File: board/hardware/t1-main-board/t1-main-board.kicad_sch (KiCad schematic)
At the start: 0 parts

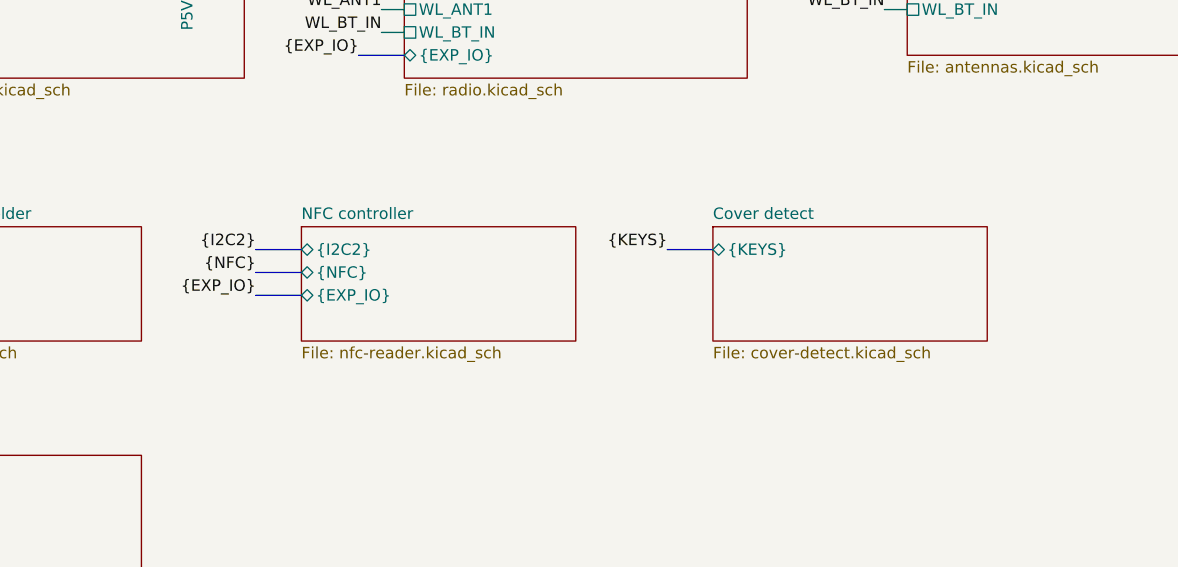
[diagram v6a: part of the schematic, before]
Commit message: NFC reader withdrawn from the board, every model (BRD-057)
Maintainer decision 2026-10-27, reason: board area. blk.nfc-reader (#42)
withdrawn: PN7160, front end, crystal, antenna contacts, NFC_VBAT switch
and link #18 removed (35 parts). BRD-057 reworded: NFC as the dynamic tag
only; blk.nfc-tag stays. Pinout v1: 1N20, A37, B38 become unconnected
spares, expander P05 a spare. BOM v1.18 item 7 (line 50: 5 switches,
lines 127-128 withdrawn), power tree v0.10, variant files, feature blocks.

Sheets after the removed one move up a page; references renumbered in
plan.py, parts.py and the specs (J6201 -> J6101 and others).

Placement v1.4: 990 parts placed, board need 96.9 % (99.1 % before),
factor 1.72; 243 capacitors within bound; DRC 0 errors; ERC 0 errors;
craft Q1 met; overlaps 0; pcb tests pass; STEP exported.

Co-Authored-By: Claude Opus 5.5 <noreply@anthropic.com>
Claude-Session: https://claude.ai/code/session_01Ei262h3TpgY9vyfNLMi5Mn
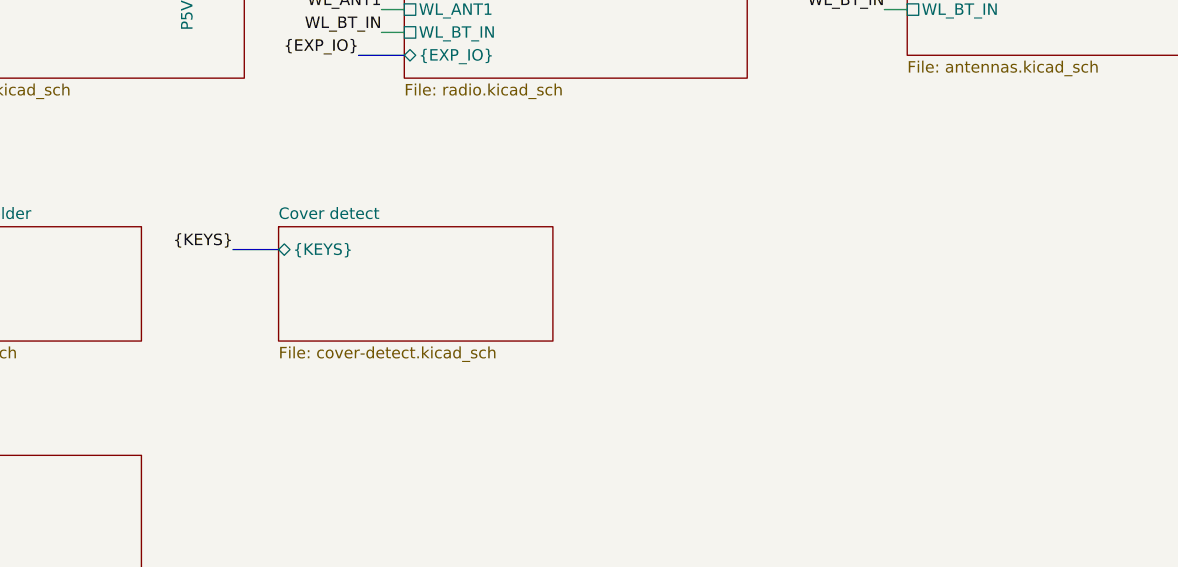
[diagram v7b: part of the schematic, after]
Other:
- removed sheet NFC controller

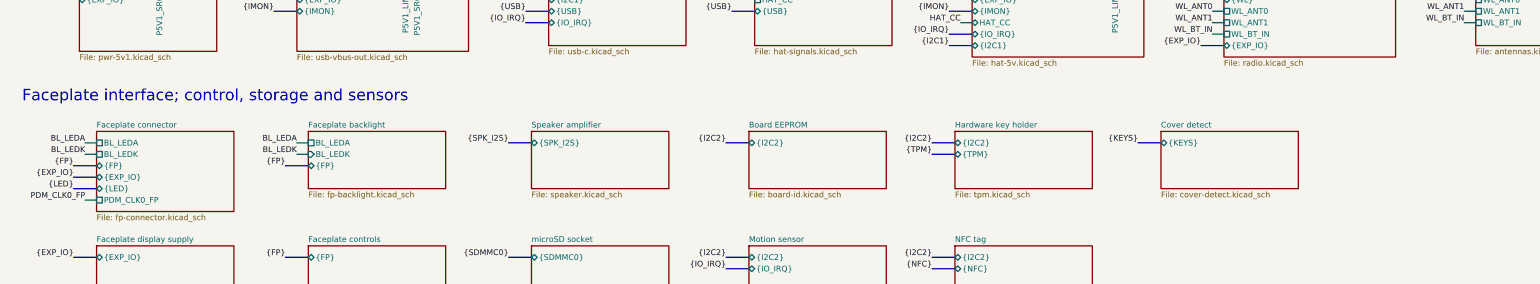
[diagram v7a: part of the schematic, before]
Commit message: Shield-can frames on the back (BOM v1.19, placement v1.6)
blk.shields: three etched two-piece frames made to order under the
amended T1-038, not fitted in either variant: SoC and LPDDR4X, the radio
module, the DACs and the back of the headphone stage. shields.toml holds
the geometry; pcb/shields.py derives land, keep-outs and courtyard ring;
the generator draws the lands and the placer reserves them, with parts up
to 1.3 mm inside (PCB-Z-01). The sheet takes page 59, so the sheets from
fp-display on carry the next page (J6201, SW6901-SW6904).

Placement v1.6: 994 parts placed, 99.5 % board need (97.0 % before the
frames), factor 1.64, 244 capacitors within their bound, DRC 0 errors,
ERC 0 errors, craft Q1 met, pcb tests pass (31), STEP exported.

Co-Authored-By: Claude Opus 5.5 <noreply@anthropic.com>
Claude-Session: https://claude.ai/code/session_013P6pW9LdyEMFishwCcZGUr
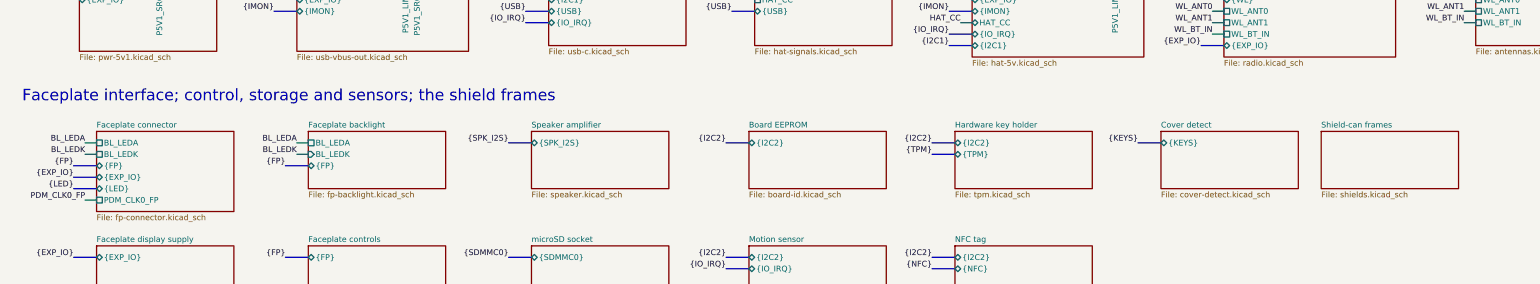
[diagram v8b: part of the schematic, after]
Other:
- added sheet Shield-can frames (shields.kicad_sch)
- note added: "Faceplate interface; control, storage and sensors; the shield frames"
- note removed: "Faceplate interface; control, storage and sensors"
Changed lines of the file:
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@@
 (text "SoC, memory, the coprocessor and MaskROM entry; audio, from the DACs to the jacks; instrumentation and debug" (exclude_from_sim no) (at 25.4 81.28 0) (effects (font (size 2.54 2.54)) (justify left bottom)))
 (text "USB ports (the 5.1 V source, USB-C, the HAT port) and the radio" (exclude_from_sim no) (at 25.4 162.56 0) (effects (font (size 2.54 2.54)) (justify left bottom)))
-(text "Faceplate interface; control, storage and sensors" (exclude_from_sim no) (at 25.4 207.01 0) (effects (font (size 2.54 2.54)) (justify left bottom)))
+(text "Faceplate interface; control, storage and sensors; the shield frames" (exclude_from_sim no) (at 25.4 207.01 0) (effects (font (size 2.54 2.54)) (justify left bottom)))
 (text_box "Notes\n1. Reading order: overviews first, then blocks left to right as power and signals flow;\n   page numbers follow it (CRAFT-111). The SoC's sub-sheets follow the SoC.\n2. Rails cross the hierarchy as power symbols named as the power tree; signals as sheet pins\n   named as each block's interface (CRAFT-112). Buses cross as one bus pin through the\n   project's bus aliases (DDR_CHA, DDR_CHB, EMMC); their members keep their names.\n3. Every block in use has a sheet; a net with a single pin by design ends in a local label." (exclude_from_sim no) (at 300.99 86.36 0) (size 99.06 19.05) (margins 1.905 1.905 1.905 1.905) (stroke (width 0) (type default)) (fill (type none)) (effects (font (size 1.27 1.27)) (justify left top)))
 (sheet (at 25.4 50.8) (size 30.48 12.7) (exclude_from_sim no) (in_bom yes) (on_board yes) (dnp no) (fields_autoplaced yes) (stroke (width 0.1524) (type solid)) (fill (color 0 0 0 0.0000))
@@
   (property "Block" "blk.fp-display" (at 41.91 254.588 0) (effects (font (size 1.27 1.27)) (justify left top)) (hide yes))
   (pin "{EXP_IO}" bidirectional (at 41.91 241.3 180) (effects (font (size 1.27 1.27)) (justify left)))
-  (instances (project "t1-main-board" (path "/7746052e-d7f9-59ad-ba73-bd2b74439529" (page "59"))))
+  (instances (project "t1-main-board" (path "/7746052e-d7f9-59ad-ba73-bd2b74439529" (page "60"))))
 )
 (sheet (at 88.9 213.36) (size 30.48 12.7) (exclude_from_sim no) (in_bom yes) (on_board yes) (dnp no) (fields_autoplaced yes) (stroke (width 0.1524) (type solid)) (fill (color 0 0 0 0.0000))
@@
   (property "Block" "blk.fp-controls" (at 88.9 254.588 0) (effects (font (size 1.27 1.27)) (justify left top)) (hide yes))
   (pin "{FP}" bidirectional (at 88.9 241.3 180) (effects (font (size 1.27 1.27)) (justify left)))
-  (instances (project "t1-main-board" (path "/7746052e-d7f9-59ad-ba73-bd2b74439529" (page "60"))))
+  (instances (project "t1-main-board" (path "/7746052e-d7f9-59ad-ba73-bd2b74439529" (page "61"))))
 )
 (sheet (at 41.91 259.08) (size 30.48 12.7) (exclude_from_sim no) (in_bom yes) (on_board yes) (dnp no) (fields_autoplaced yes) (stroke (width 0.1524) (type solid)) (fill (color 0 0 0 0.0000))
@@
   (pin "{FP}" bidirectional (at 41.91 261.62 180) (effects (font (size 1.27 1.27)) (justify left)))
   (pin "PDM_CLK0_FP" passive (at 41.91 264.16 180) (effects (font (size 1.27 1.27)) (justify left)))
-  (instances (project "t1-main-board" (path "/7746052e-d7f9-59ad-ba73-bd2b74439529" (page "64"))))
+  (instances (project "t1-main-board" (path "/7746052e-d7f9-59ad-ba73-bd2b74439529" (page "65"))))
 )
 (sheet (at 138.43 259.08) (size 30.48 12.7) (exclude_from_sim no) (in_bom yes) (on_board yes) (dnp no) (fields_autoplaced yes) (stroke (width 0.1524) (type solid)) (fill (color 0 0 0 0.0000))
@@
   (pin "{IO_IRQ}" bidirectional (at 138.43 264.16 180) (effects (font (size 1.27 1.27)) (justify left)))
   (pin "{I2C2}" bidirectional (at 138.43 266.7 180) (effects (font (size 1.27 1.27)) (justify left)))
-  (instances (project "t1-main-board" (path "/7746052e-d7f9-59ad-ba73-bd2b74439529" (page "66"))))
+  (instances (project "t1-main-board" (path "/7746052e-d7f9-59ad-ba73-bd2b74439529" (page "67"))))
 )
 (sheet (at 186.69 213.36) (size 30.48 12.7) (exclude_from_sim no) (in_bom yes) (on_board yes) (dnp no) (fields_autoplaced yes) (stroke (width 0.1524) (type solid)) (fill (color 0 0 0 0.0000))
@@
   (property "Block" "blk.microsd" (at 138.43 254.588 0) (effects (font (size 1.27 1.27)) (justify left top)) (hide yes))
   (pin "{SDMMC0}" bidirectional (at 138.43 241.3 180) (effects (font (size 1.27 1.27)) (justify left)))
-  (instances (project "t1-main-board" (path "/7746052e-d7f9-59ad-ba73-bd2b74439529" (page "61"))))
+  (instances (project "t1-main-board" (path "/7746052e-d7f9-59ad-ba73-bd2b74439529" (page "62"))))
 )
 (sheet (at 186.69 238.76) (size 30.48 12.7) (exclude_from_sim no) (in_bom yes) (on_board yes) (dnp no) (fields_autoplaced yes) (stroke (width 0.1524) (type solid)) (fill (color 0 0 0 0.0000))
@@
   (pin "{I2C2}" bidirectional (at 186.69 241.3 180) (effects (font (size 1.27 1.27)) (justify left)))
   (pin "{IO_IRQ}" bidirectional (at 186.69 243.84 180) (effects (font (size 1.27 1.27)) (justify left)))
-  (instances (project "t1-main-board" (path "/7746052e-d7f9-59ad-ba73-bd2b74439529" (page "62"))))
+  (instances (project "t1-main-board" (path "/7746052e-d7f9-59ad-ba73-bd2b74439529" (page "63"))))
 )
 (sheet (at 138.43 213.36) (size 30.48 12.7) (exclude_from_sim no) (in_bom yes) (on_board yes) (dnp no) (fields_autoplaced yes) (stroke (width 0.1524) (type solid)) (fill (color 0 0 0 0.0000))
@@
   (pin "{EXP_IO}" bidirectional (at 186.69 261.62 180) (effects (font (size 1.27 1.27)) (justify left)))
   (pin "{I2C2}" bidirectional (at 186.69 264.16 180) (effects (font (size 1.27 1.27)) (justify left)))
-  (instances (project "t1-main-board" (path "/7746052e-d7f9-59ad-ba73-bd2b74439529" (page "67"))))
+  (instances (project "t1-main-board" (path "/7746052e-d7f9-59ad-ba73-bd2b74439529" (page "68"))))
 )
 (sheet (at 232.41 213.36) (size 30.48 12.7) (exclude_from_sim no) (in_bom yes) (on_board yes) (dnp no) (fields_autoplaced yes) (stroke (width 0.1524) (type solid)) (fill (color 0 0 0 0.0000))
@@
   (pin "{I2C2}" bidirectional (at 232.41 241.3 180) (effects (font (size 1.27 1.27)) (justify left)))
   (pin "{NFC}" bidirectional (at 232.41 243.84 180) (effects (font (size 1.27 1.27)) (justify left)))
-  (instances (project "t1-main-board" (path "/7746052e-d7f9-59ad-ba73-bd2b74439529" (page "63"))))
+  (instances (project "t1-main-board" (path "/7746052e-d7f9-59ad-ba73-bd2b74439529" (page "64"))))
 )
 (sheet (at 232.41 259.08) (size 30.48 12.7) (exclude_from_sim no) (in_bom yes) (on_board yes) (dnp no) (fields_autoplaced yes) (stroke (width 0.1524) (type solid)) (fill (color 0 0 0 0.0000))
@@
   (property "Block" "blk.buttons" (at 232.41 274.908 0) (effects (font (size 1.27 1.27)) (justify left top)) (hide yes))
   (pin "{KEYS}" bidirectional (at 232.41 261.62 180) (effects (font (size 1.27 1.27)) (justify left)))
-  (instances (project "t1-main-board" (path "/7746052e-d7f9-59ad-ba73-bd2b74439529" (page "68"))))
+  (instances (project "t1-main-board" (path "/7746052e-d7f9-59ad-ba73-bd2b74439529" (page "69"))))
 )
 (sheet (at 265.43 106.68) (size 30.48 12.7) (exclude_from_sim no) (in_bom yes) (on_board yes) (dnp no) (fields_autoplaced yes) (stroke (width 0.1524) (type solid)) (fill (color 0 0 0 0.0000))
@@
   (pin "{I2C2}" bidirectional (at 88.9 261.62 180) (effects (font (size 1.27 1.27)) (justify left)))
   (pin "{LED}" bidirectional (at 88.9 264.16 180) (effects (font (size 1.27 1.27)) (justify left)))
-  (instances (project "t1-main-board" (path "/7746052e-d7f9-59ad-ba73-bd2b74439529" (page "65"))))
+  (instances (project "t1-main-board" (path "/7746052e-d7f9-59ad-ba73-bd2b74439529" (page "66"))))
 )
 (sheet (at 363.22 132.08) (size 30.48 12.7) (exclude_from_sim no) (in_bom yes) (on_board yes) (dnp no) (fields_autoplaced yes) (stroke (width 0.1524) (type solid)) (fill (color 0 0 0 0.0000))
@@
   (instances (project "t1-main-board" (path "/7746052e-d7f9-59ad-ba73-bd2b74439529" (page "41"))))
 )
+(sheet (at 313.69 213.36) (size 30.48 12.7) (exclude_from_sim no) (in_bom yes) (on_board yes) (dnp no) (fields_autoplaced yes) (stroke (width 0.1524) (type solid)) (fill (color 0 0 0 0.0000))
+  (property "Sheetname" "Shield-can frames" (at 313.69 212.648 0) (effects (font (size 1.27 1.27)) (justify left bottom)))
+  (property "Sheetfile" "shields.kicad_sch" (at 313.69 226.648 0) (effects (font (size 1.27 1.27)) (justify left top)))
+  (property "Block" "blk.shields" (at 313.69 229.188 0) (effects (font (size 1.27 1.27)) (justify left top)) (hide yes))
+  (instances (project "t1-main-board" (path "/7746052e-d7f9-59ad-ba73-bd2b74439529" (page "59"))))
+)
 (wire (pts (xy 109.22 53.34) (xy 106.68 53.34)) (stroke (width 0) (type default)))
